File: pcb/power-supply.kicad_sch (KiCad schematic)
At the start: 25 parts, among them IC1 AP2112K-3.3TRG1, IC3 INA199B2, IC4 AP62300TWU-7

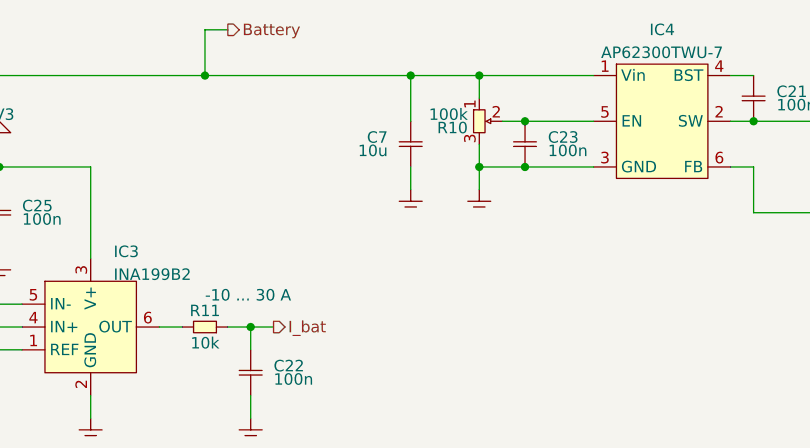
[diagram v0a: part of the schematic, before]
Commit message: added resistor to tweak step-down low-voltage range. flipped trimmer polarity
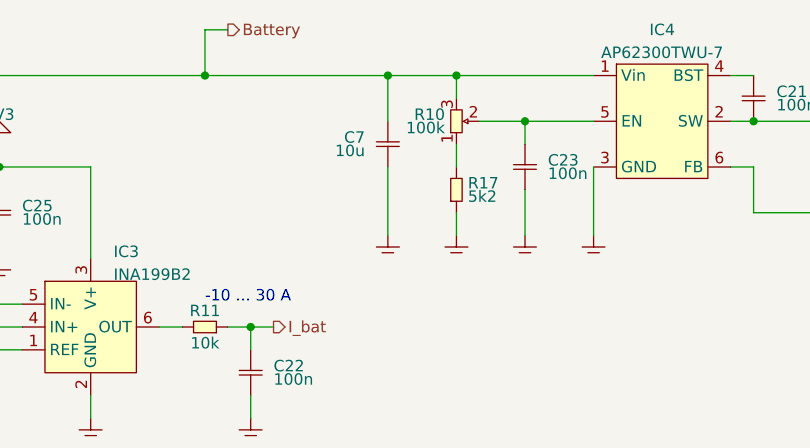
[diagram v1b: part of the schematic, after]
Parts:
- added R17: 5k2, SMT:0603, symbol generic:R
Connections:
- net Battery: now also R10.3; no longer R10.1
- net GND: now also R17.1; no longer R10.3
- new net: R10.1, R17.2
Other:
- moved on the sheet: C23, C7, R10

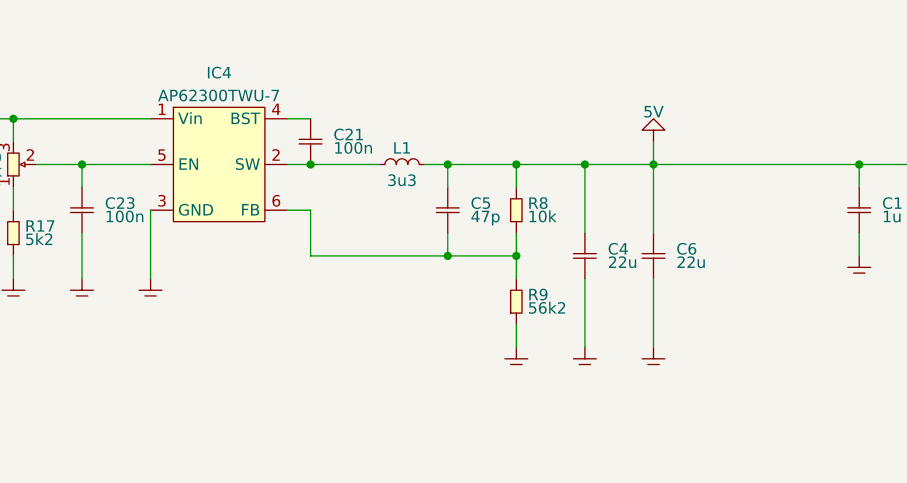
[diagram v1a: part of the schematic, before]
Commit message: circuit seems to kill buck module at 14 V. even when installed as a dead bug
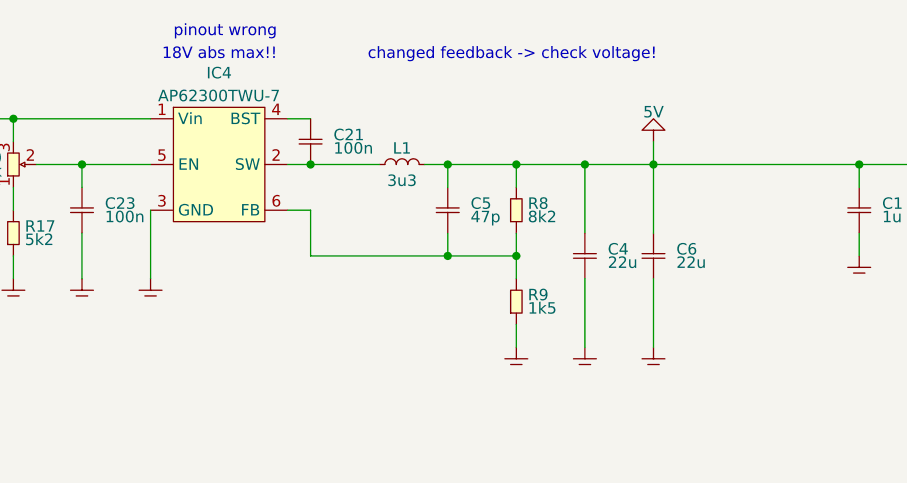
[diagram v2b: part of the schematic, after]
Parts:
- R8: value 10k -> 8k2
- R9: value 56k2 -> 1k5
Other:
- note added: "18V abs max!!"
- note added: "changed feedback -> check voltage!"
- note added: "pinout wrong"
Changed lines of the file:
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@@
+    (effects (font (size 1.27 1.27)) (justify left bottom))
+  )
+  (text "changed feedback -> check voltage!" (at 168.91 87.63 0)
+    (effects (font (size 1.27 1.27)) (justify left bottom))
+  )
+  (text "18V abs max!!" (at 146.05 87.63 0)
+    (effects (font (size 1.27 1.27)) (justify left bottom))
+  )
+  (text "pinout wrong" (at 147.32 85.09 0)
     (effects (font (size 1.27 1.27)) (justify left bottom))
   )
@@
       (effects (font (size 1.27 1.27)) (justify right top))
     )
-    (property "Value" "56k2" (at 186.69 114.3 90)
+    (property "Value" "1k5" (at 186.69 114.3 90)
       (effects (font (size 1.27 1.27)) (justify right bottom))
     )
@@
       (effects (font (size 1.27 1.27)) (justify right top))
     )
-    (property "Value" "10k" (at 186.69 104.14 90)
+    (property "Value" "8k2" (at 186.69 104.14 90)
       (effects (font (size 1.27 1.27)) (justify right bottom))
     )

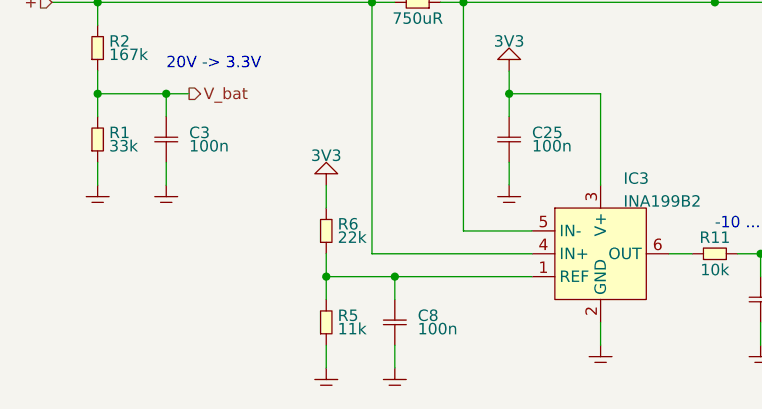
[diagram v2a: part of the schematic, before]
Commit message: changed current measurement offset resistor values
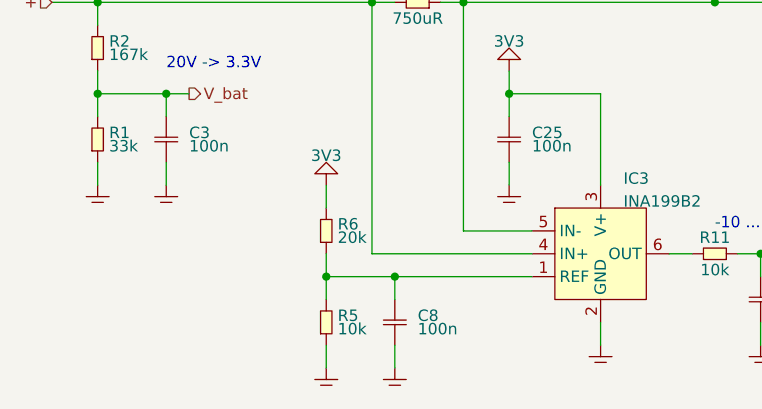
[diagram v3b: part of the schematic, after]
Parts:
- R5: value 11k -> 10k
- R6: value 22k -> 20k
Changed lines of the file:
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@@
       (effects (font (size 1.27 1.27)) (justify right top))
     )
-    (property "Value" "11k" (at 59.69 129.54 90)
+    (property "Value" "10k" (at 59.69 129.54 90)
       (effects (font (size 1.27 1.27)) (justify right bottom))
     )
@@
       (effects (font (size 1.27 1.27)) (justify right top))
     )
-    (property "Value" "22k" (at 59.69 119.38 90)
+    (property "Value" "20k" (at 59.69 119.38 90)
       (effects (font (size 1.27 1.27)) (justify right bottom))
     )

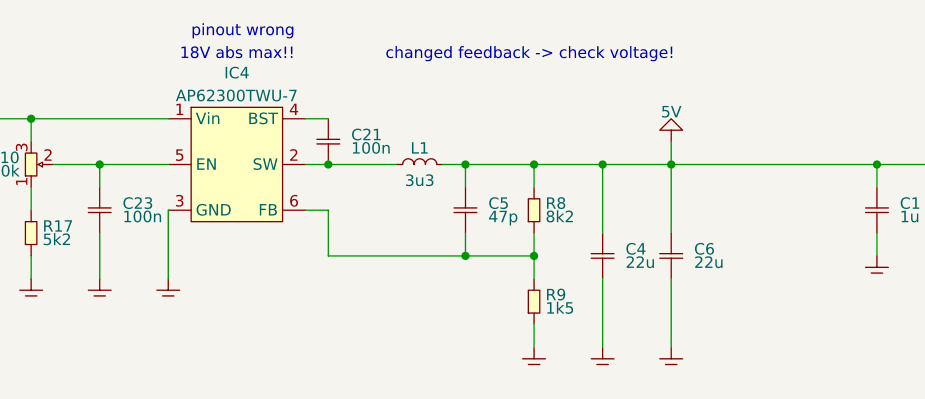
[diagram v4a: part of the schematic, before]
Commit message: worked on layout. changed step-down module
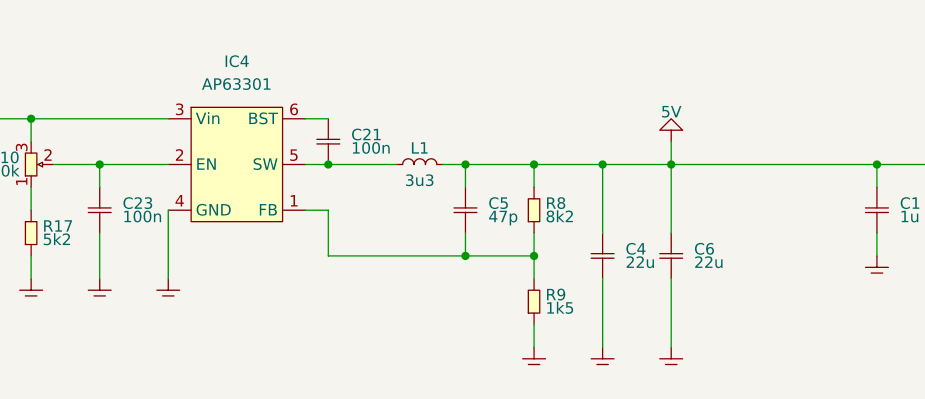
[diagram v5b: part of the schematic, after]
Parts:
- removed IC4: AP62300TWU-7, SOT:SOT-23-6, symbol Power:AP62300TWU-7
- added IC4: AP63301, TSOT:TSOT-26, symbol Power:AP63301WU-7
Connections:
- net Battery: now also IC4.3 (Vin)
- net GND: now also IC4.4 (GND)
- net at C23.1, R10.2: now also IC4.2 (EN)
- net at C21.1: now also IC4.6 (BST)
- net at C21.2, L1.1: now also IC4.5 (SW)
- net at C5.2, R8.1, R9.2: now also IC4.1 (FB)
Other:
- note removed: "18V abs max!!"
- note removed: "changed feedback -> check voltage!"
- note removed: "pinout wrong"
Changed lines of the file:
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@@
 		)
 	)
-	(text "changed feedback -> check voltage!"
-		(exclude_from_sim no)
-		(at 168.91 87.63 0)
-		(effects
-			(font
-				(size 1.27 1.27)
-			)
-			(justify left bottom)
-		)
-	)
-	(text "18V abs max!!"
-		(exclude_from_sim no)
-		(at 146.05 87.63 0)
-		(effects
-			(font
-				(size 1.27 1.27)
-			)
-			(justify left bottom)
-		)
-	)
-	(text "pinout wrong"
-		(exclude_from_sim no)
-		(at 147.32 85.09 0)
-		(effects
-			(font
-				(size 1.27 1.27)
-			)
-			(justify left bottom)
-		)
-	)
 	(text "20V -> 3.3V"
 		(exclude_from_sim no)
@@
 	)
 	(symbol
-		(lib_id "Power:AP62300TWU-7")
+		(lib_id "Power:AP63301WU-7")
 		(at 152.4 99.06 0)
 		(unit 1)
@@
 		(fields_autoplaced yes)
 		(property "Reference" "IC4"
-			(at 152.4 88.9 0)
+			(at 152.4 87.63 0)
 			(effects
 				(font
@@
 			)
 		)
-		(property "Value" "AP62300TWU-7"
-			(at 152.4 91.44 0)
+		(property "Value" "AP63301"
+			(at 152.4 90.17 0)
 			(effects
 				(font
@@
 			)
 		)
-		(property "Footprint" "SOT:SOT-23-6"
-			(at 161.036 95.504 0)
+		(property "Footprint" "TSOT:TSOT-26"
+			(at 156.718 83.566 0)
 			(effects
 				(font
@@
 			)
 		)
-		(property "Datasheet" "https://www.diodes.com/assets/Datasheets/AP62300_AP62301_AP62300T.pdf"
-			(at 148.59 93.98 0)
+		(property "Datasheet" "https://www.diodes.com/assets/Datasheets/AP63300-AP63301.pdf"
+			(at 159.004 86.106 0)
 			(effects
 				(font
@@
 			)
 		)
-		(property "Description" ""
-			(at 152.4 99.06 0)
+		(property "Description" "3.8V TO 32V INPUT, 3A LOW IQ SYNCHRONOUS BUCK WITH ENHANCED EMI REDUCTION"
+			(at 150.876 86.106 0)
 			(effects
 				(font
@@
 			)
 		)
-		(property "MPN" "AP62300TWU-7"
-			(at 152.4 99.06 0)
+		(property "MPN" "AP63301WU-7"
+			(at 152.908 85.852 0)
 			(effects
 				(font
@@
 			)
 		)
-		(property "DigiKey" "31-AP62300TWU-7CT-ND"
-			(at 152.4 99.06 0)
+		(property "DigiKey" "31-AP63301WU-7CT-ND"
+			(at 151.13 85.598 0)
 			(effects
 				(font
@@
 		)
 		(property "Manufacturer" "Diodes Incorporated"
-			(at 152.4 99.06 0)
+			(at 152.4 85.852 0)
 			(effects
 				(font
@@
 		(pin "3"
 		)
-		(pin "4"
-		)
 		(pin "5"
 		)
+		(pin "4"
+		)
 		(pin "6"
 		)
 		(instances
-			(project "pcb"
+			(project ""
 				(path "/6bb3bad6-1a89-4624-b34d-6ddda7dd16d2/bd5ce3a2-965f-4825-a529-9d15232fee93"
 					(reference "IC4")
